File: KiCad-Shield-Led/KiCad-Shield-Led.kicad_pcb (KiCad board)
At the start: 2 copper layers, 68.6 x 53.3 mm, 16 parts, among them P1 Power, P2 Analog, P3 Digital, P4 Digital, P5 CONN_01X01, P6 CONN_01X01, P7 CONN_01X01, P8 CONN_01X01

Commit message: Place components
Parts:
- moved D3 98.7 mm to (116.0, 104.0)
- moved D1 86.7 mm to (116.0, 86.0)
- moved D4 79.5 mm to (116.0, 113.0)
- moved R3 74.7 mm to (126.0, 104.0)
- moved D2 73.5 mm to (116.0, 95.0)
- moved R1 61.8 mm to (126.0, 86.0)
- moved R4 61.6 mm to (126.0, 113.0)
- moved R2 61.2 mm to (126.0, 95.0)
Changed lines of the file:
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@@
   (general
     (thickness 1.6)
-    (drawings 27)
+    (drawings 28)
     (tracks 0)
     (zones 0)
@@
     (pad_drill 3.048)
     (pad_to_mask_clearance 0)
-    (aux_axis_origin 110.998 126.365)
-    (grid_origin 110.998 126.365)
+    (aux_axis_origin 110.998 73.025)
+    (grid_origin 110.998 73.025)
     (visible_elements 7FFFFFFF)
     (pcbplotparams
@@
   )
   (module LED_THT:LED_D5.0mm (layer F.Cu)
-    (at 201.213001 101.940001)
+    (at 115.998 86.025)
     (descr "LED, diameter 5.0mm, 2 pins, http://cdn-reichelt.de/documents/datenblatt/A500/LL-504BC2E-009.pdf")
     (tags "LED diameter 5.0mm 2 pins")
@@
   )
   (module LED_THT:LED_D5.0mm (layer F.Cu)
-    (at 187.903001 110.040001)
+    (at 115.998 95.025)
     (descr "LED, diameter 5.0mm, 2 pins, http://cdn-reichelt.de/documents/datenblatt/A500/LL-504BC2E-009.pdf")
     (tags "LED diameter 5.0mm 2 pins")
@@
   )
   (module LED_THT:LED_D5.0mm (layer F.Cu)
-    (at 214.523001 97.890001)
+    (at 115.998 104.025)
     (descr "LED, diameter 5.0mm, 2 pins, http://cdn-reichelt.de/documents/datenblatt/A500/LL-504BC2E-009.pdf")
     (tags "LED diameter 5.0mm 2 pins")
@@
   )
   (module LED_THT:LED_D5.0mm (layer F.Cu)
-    (at 195.403001 110.040001)
+    (at 115.998 113.025)
     (descr "LED, diameter 5.0mm, 2 pins, http://cdn-reichelt.de/documents/datenblatt/A500/LL-504BC2E-009.pdf")
     (tags "LED diameter 5.0mm 2 pins")
@@
   )
   (module Resistor_THT:R_Axial_DIN0207_L6.3mm_D2.5mm_P10.16mm_Horizontal (layer F.Cu)
-    (at 187.003001 96.140001)
+    (at 125.998 86.025)
     (descr "Resistor, Axial_DIN0207 series, Axial, Horizontal, pin pitch=10.16mm, 0.25W = 1/4W, length*diameter=6.3*2.5mm^2, http://cdn-reichelt.de/documents/datenblatt/B400/1_4W%23YAG.pdf")
     (tags "Resistor Axial_DIN0207 series Axial Horizontal pin pitch 10.16mm 0.25W = 1/4W length 6.3mm diameter 2.5mm")
@@
   )
   (module Resistor_THT:R_Axial_DIN0207_L6.3mm_D2.5mm_P10.16mm_Horizontal (layer F.Cu)
-    (at 187.003001 100.190001)
+    (at 125.998 95.025)
     (descr "Resistor, Axial_DIN0207 series, Axial, Horizontal, pin pitch=10.16mm, 0.25W = 1/4W, length*diameter=6.3*2.5mm^2, http://cdn-reichelt.de/documents/datenblatt/B400/1_4W%23YAG.pdf")
     (tags "Resistor Axial_DIN0207 series Axial Horizontal pin pitch 10.16mm 0.25W = 1/4W length 6.3mm diameter 2.5mm")
@@
   )
   (module Resistor_THT:R_Axial_DIN0207_L6.3mm_D2.5mm_P10.16mm_Horizontal (layer F.Cu)
-    (at 200.313001 96.140001)
+    (at 125.998 104.025)
     (descr "Resistor, Axial_DIN0207 series, Axial, Horizontal, pin pitch=10.16mm, 0.25W = 1/4W, length*diameter=6.3*2.5mm^2, http://cdn-reichelt.de/documents/datenblatt/B400/1_4W%23YAG.pdf")
     (tags "Resistor Axial_DIN0207 series Axial Horizontal pin pitch 10.16mm 0.25W = 1/4W length 6.3mm diameter 2.5mm")
@@
   )
   (module Resistor_THT:R_Axial_DIN0207_L6.3mm_D2.5mm_P10.16mm_Horizontal (layer F.Cu)
-    (at 187.003001 104.240001)
+    (at 125.998 113.025)
     (descr "Resistor, Axial_DIN0207 series, Axial, Horizontal, pin pitch=10.16mm, 0.25W = 1/4W, length*diameter=6.3*2.5mm^2, http://cdn-reichelt.de/documents/datenblatt/B400/1_4W%23YAG.pdf")
     (tags "Resistor Axial_DIN0207 series Axial Horizontal pin pitch 10.16mm 0.25W = 1/4W length 6.3mm diameter 2.5mm")
@@
     )
   )
+  (dimension 10 (width 0.15) (layer Dwgs.User)
+    (gr_text "10.000 mm" (at 124.938 80.565 270) (layer Dwgs.User)
+      (effects (font (size 1 1) (thickness 0.15)))
+    )
+    (feature1 (pts (xy 126.238 85.565) (xy 125.651579 85.565)))
+    (feature2 (pts (xy 126.238 75.565) (xy 125.651579 75.565)))
+    (crossbar (pts (xy 126.238 75.565) (xy 126.238 85.565)))
+    (arrow1a (pts (xy 126.238 85.565) (xy 125.651579 84.438496)))
+    (arrow1b (pts (xy 126.238 85.565) (xy 126.824421 84.438496)))
+    (arrow2a (pts (xy 126.238 75.565) (xy 125.651579 76.691504)))
+    (arrow2b (pts (xy 126.238 75.565) (xy 126.824421 76.691504)))
+  )
   (gr_text 1 (at 138.938 121.285 90) (layer F.SilkS)

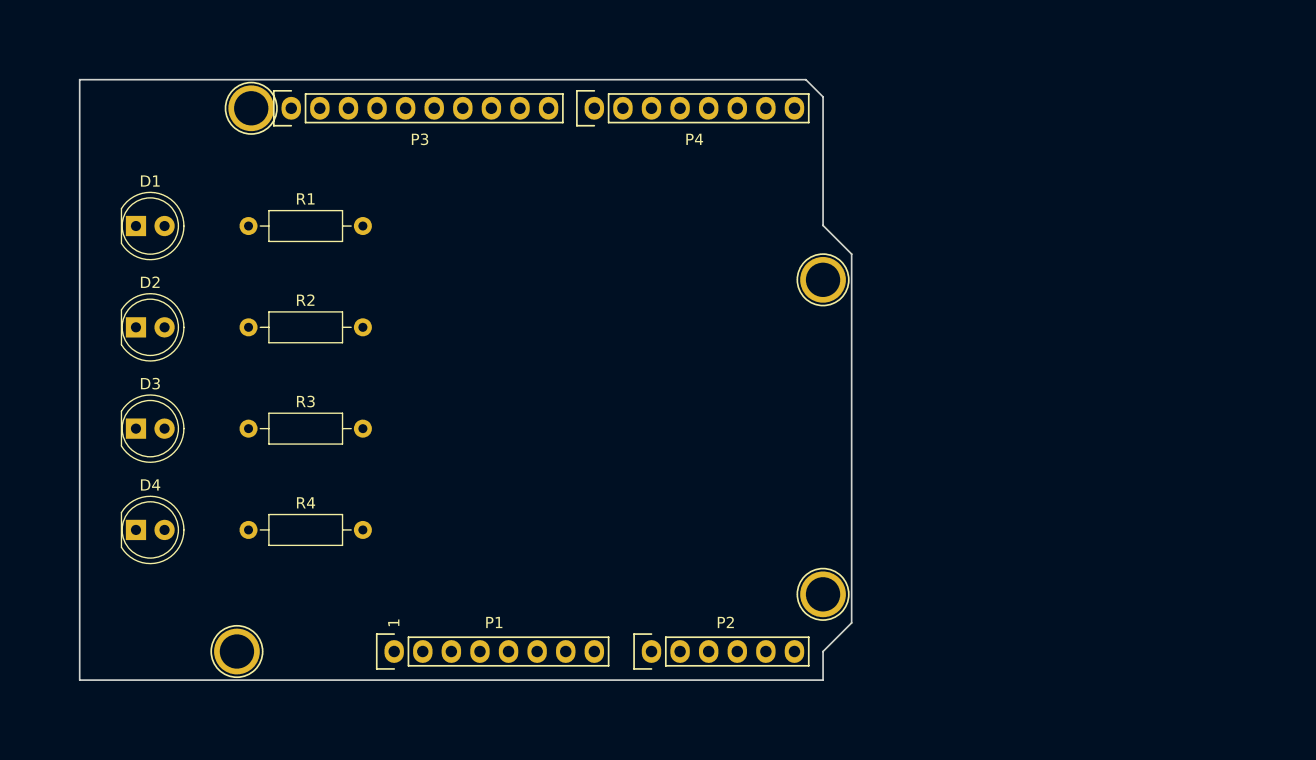
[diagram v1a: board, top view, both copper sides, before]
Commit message: Routage des signaux de la carte
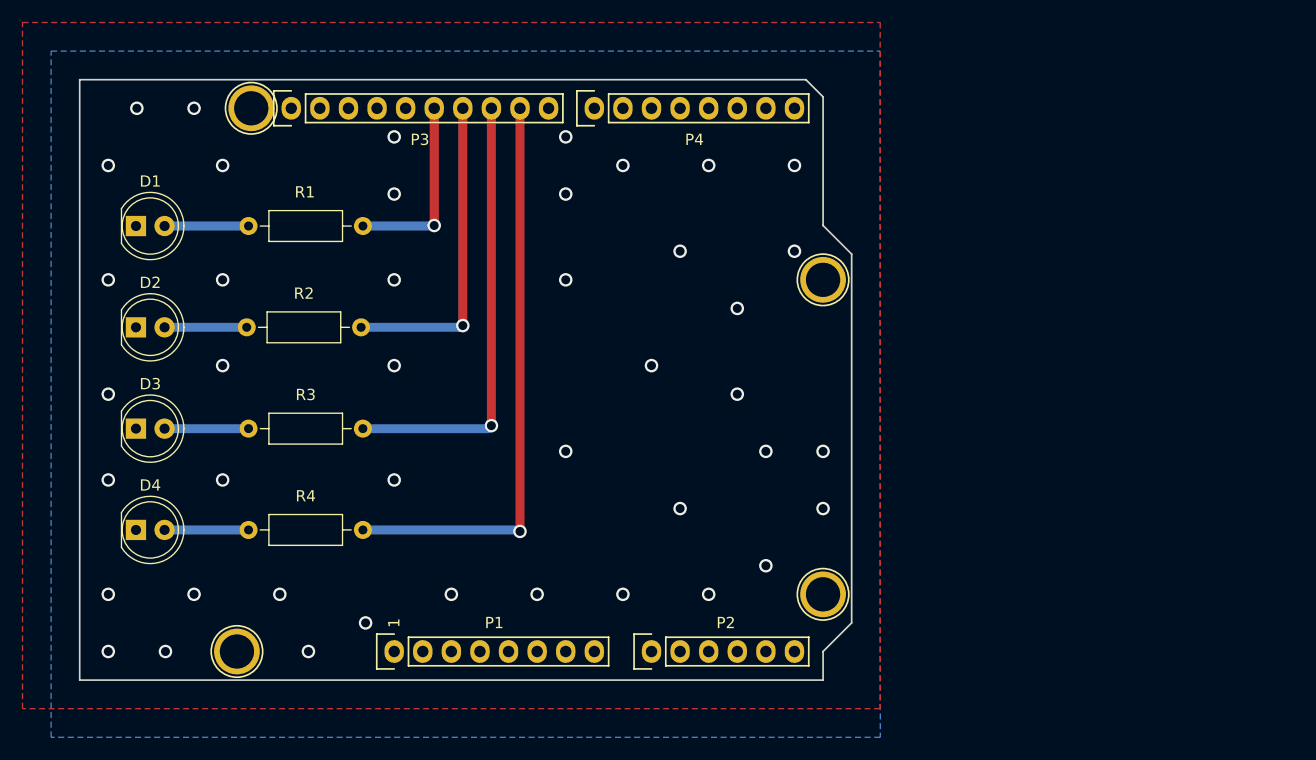
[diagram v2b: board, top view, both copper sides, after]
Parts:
- moved R1 10.2 mm to (136.2, 86.0), turned to 180 degrees
- moved R3 10.2 mm to (136.2, 104.0), turned to 180 degrees
- moved R4 10.2 mm to (136.2, 113.0), turned to 180 degrees
- moved R2 10.00 mm to (136.0, 95.0), turned to 180 degrees
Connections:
- P3 pad 1: /A5(SCL) -> Net-(P3-Pad1)
- P3 pad 2: /A4(SDA) -> Net-(P3-Pad2)
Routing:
- net /LED4: track 0.00 -> 51.6 mm, vias 0 -> 1
- net /LED3: track 0.00 -> 39.7 mm, vias 0 -> 1
- net /LED2: track 0.00 -> 28.4 mm, vias 0 -> 1
- net /LED1: track 0.00 -> 16.8 mm, vias 0 -> 1
- net Net-(D4-Pad2): track 0.00 -> 7.46 mm
- net Net-(D3-Pad2): track 0.00 -> 7.46 mm
- net Net-(D1-Pad2): track 0.00 -> 7.46 mm
- net Net-(D2-Pad2): track 0.00 -> 7.30 mm
- net GND: vias 0 -> 43
- added copper zone on B.Cu, net GND
- added copper zone on F.Cu, net GND

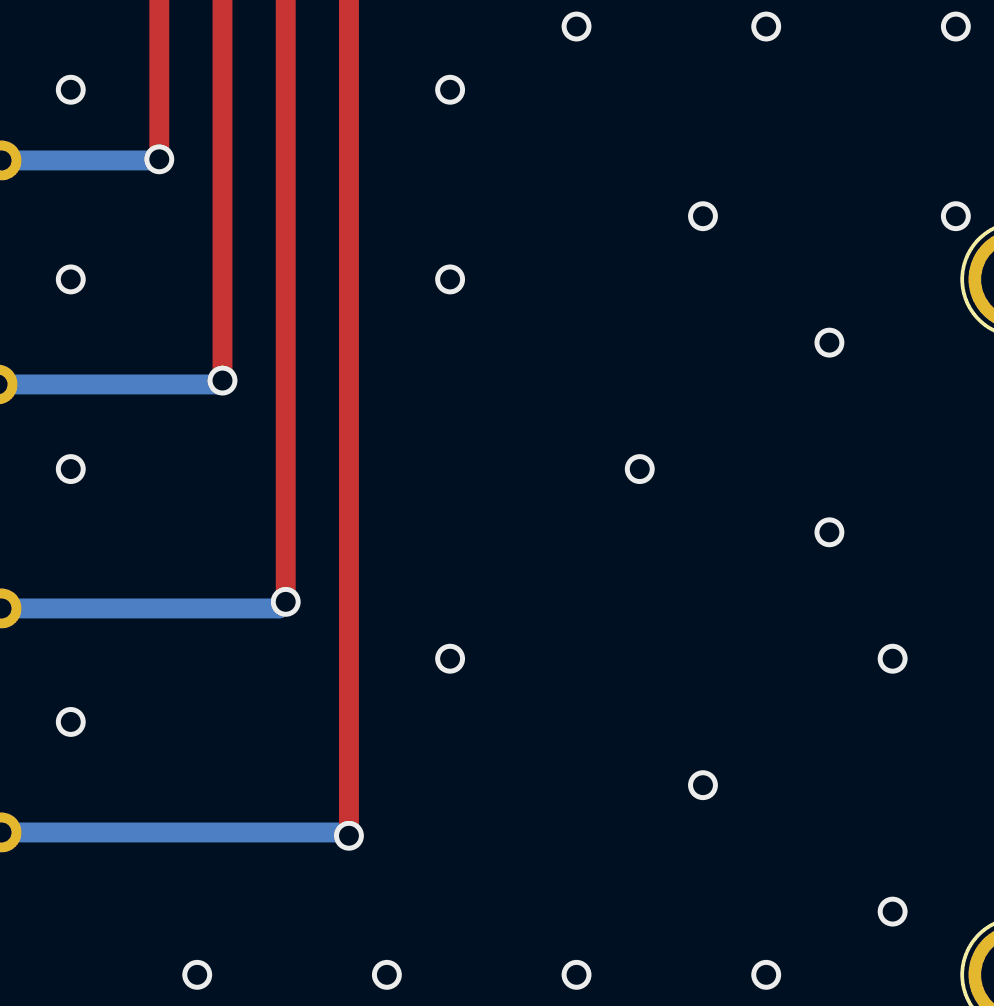
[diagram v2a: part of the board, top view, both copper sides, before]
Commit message: Ajout du modele 3D de notre librairie GazSensor
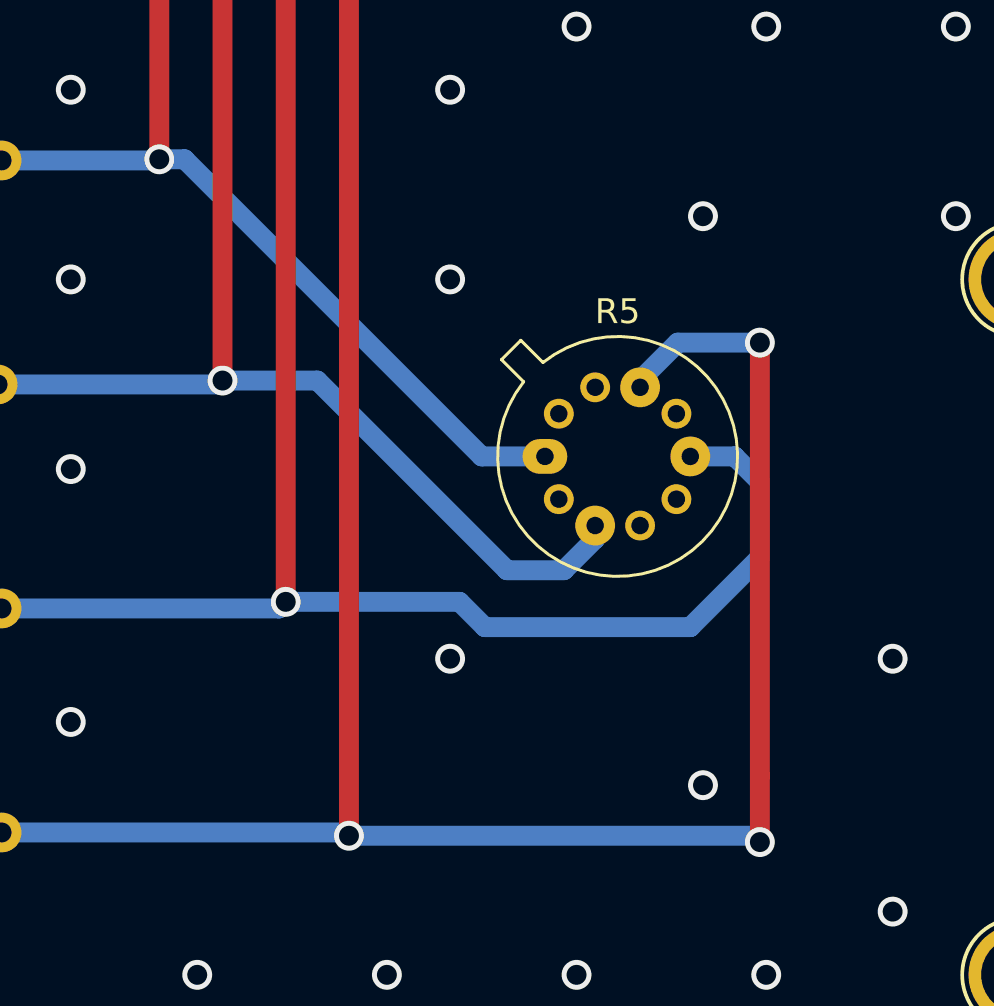
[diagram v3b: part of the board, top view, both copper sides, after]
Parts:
- added R5: Gsens, MesEmpreintes:TO-5-10_Window, F.Cu at (158.0, 97.9)
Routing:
- net /LED4: track 51.6 -> 94.0 mm, vias 1 -> 3
- net /LED3: track 39.7 -> 66.6 mm
- net /LED1: track 16.8 -> 37.2 mm
- net /LED2: track 28.4 -> 47.6 mm
- net GND: vias 43 -> 40
